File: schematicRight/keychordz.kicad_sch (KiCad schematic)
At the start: 66 parts, among them IC1 MCP73833-BZI_UN, IC2 TPS7A2024PDBVR, IC3 STM32WB55RGV7, J1 USB_C_Receptacle_USB2.0, J2 DEBUG_CONN, J3 OLED_CONN, Q1 Q_PMOS_GSD, SW1 SW_Push, SW2 SW_Push, SW3 SW_Push, SW4 SW_Push, SW5 SW_Push, SW6 SW_Push, SW7 SW_Push, SW9 SW_SPST, U1 MIC5504-3.3YM5, Y1 Crystal_GND23, Y2 Crystal

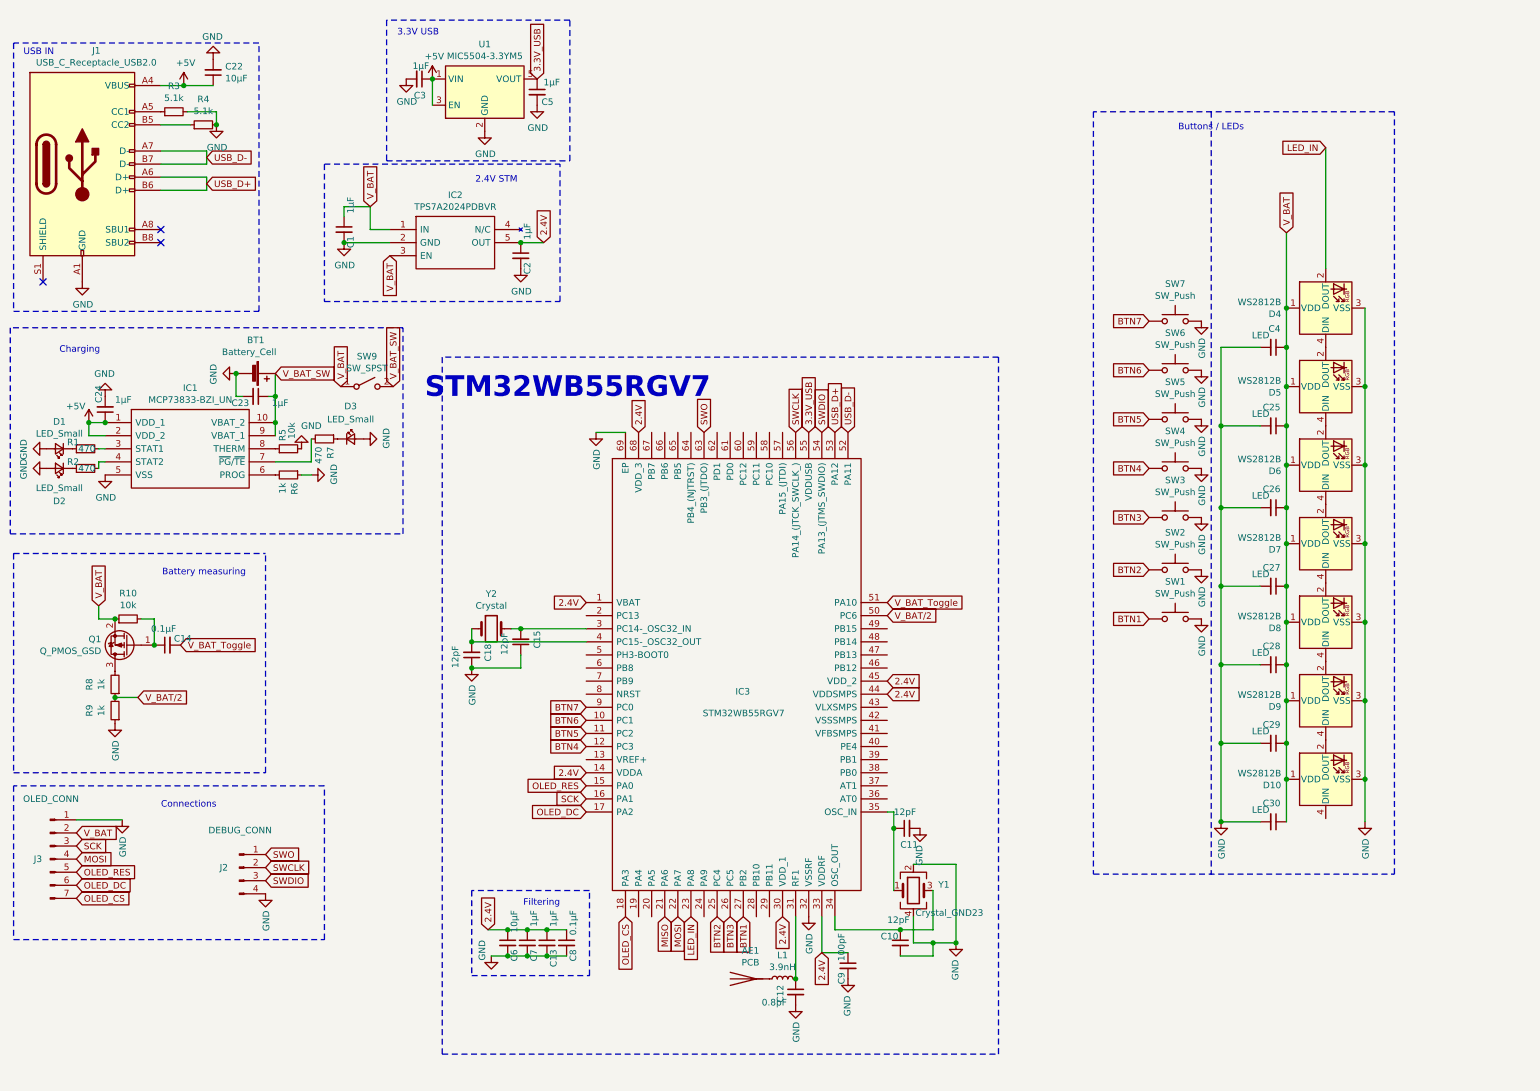
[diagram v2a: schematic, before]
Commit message: use Arduino pro micro
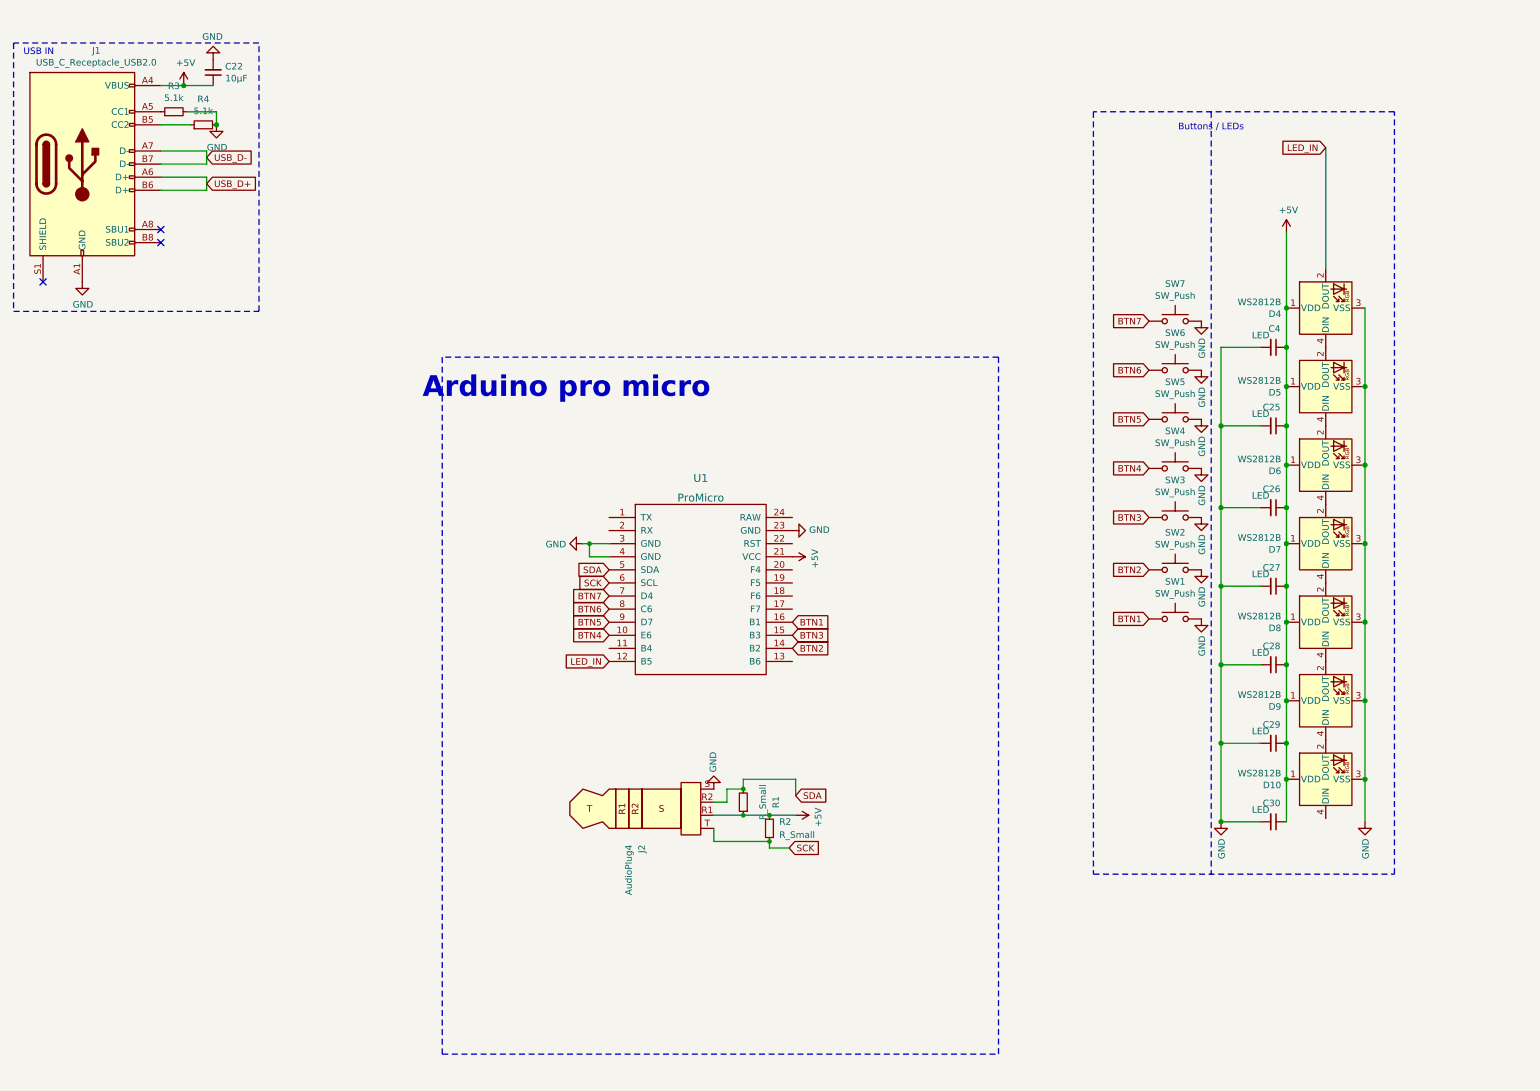
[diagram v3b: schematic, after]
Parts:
- removed AE1: PCB, RF_Antenna:Texas_SWRA117D_2.4GHz_Left, symbol Device:Antenna
- removed BT1: Battery_Cell, Battery:BatteryHolder_MPD_BH-18650-PC2, symbol Device:Battery_Cell
- removed C1, C13, C2, C23, C24, C3, C5, C7: 1µF, Capacitor_SMD:C_0402_1005Metric_Pad0.74x0.62mm_HandSolder, symbol Device:C_Small
- removed C10, C11, C15, C18: 12pF, Capacitor_SMD:C_0603_1608Metric_Pad1.08x0.95mm_HandSolder, symbol Device:C_Small
- removed C12: 0.8pF, Capacitor_SMD:C_0201_0603Metric_Pad0.64x0.40mm_HandSolder, symbol Device:C_Small
- removed C14, C8: 0.1µF, Capacitor_SMD:C_0402_1005Metric_Pad0.74x0.62mm_HandSolder, symbol Device:C_Small
- removed C6: 10µF, Capacitor_SMD:C_0402_1005Metric_Pad0.74x0.62mm_HandSolder, symbol Device:C_Small
- removed C9: 100pF, Capacitor_SMD:C_0402_1005Metric_Pad0.74x0.62mm_HandSolder, symbol Device:C_Small
- removed D1, D2, D3: LED_Small, LED_SMD:LED_0603_1608Metric_Pad1.05x0.95mm_HandSolder, symbol Device:LED_Small
- removed IC1: MCP73833-BZI_UN, Package_SO:MSOP-10_3x3mm_P0.5mm, symbol LoaderParts:MCP73833-BZI_UN
- removed IC2: TPS7A2024PDBVR, SamacSys_Parts:SOT95P280X145-5N, symbol LoaderParts:TPS7A2033PDBVR
- removed IC3: STM32WB55RGV7, SamacSys_Parts:QFN40P800X800X100-69N-D, symbol LoaderParts:STM32WB55RGV7
- removed J2: DEBUG_CONN, Connector_PinHeader_2.54mm:PinHeader_1x04_P2.54mm_Vertical, symbol Connector:Conn_01x04_Male
- removed J3: OLED_CONN, Connector_PinHeader_2.54mm:PinHeader_1x07_P2.54mm_Vertical, symbol Connector:Conn_01x07_Male
- removed L1: 3.9nH, Inductor_SMD:L_0402_1005Metric_Pad0.77x0.64mm_HandSolder, symbol Device:L_Small
- removed Q1: Q_PMOS_GSD, Package_TO_SOT_SMD:SC-59_Handsoldering, symbol Device:Q_PMOS_GSD
- removed R10: 10k, Resistor_SMD:R_0603_1608Metric_Pad0.98x0.95mm_HandSolder, symbol Device:R_Small
- removed R5: 10k, Resistor_SMD:R_0402_1005Metric_Pad0.72x0.64mm_HandSolder, symbol Device:R_Small
- removed R6: 1k, Resistor_SMD:R_0402_1005Metric_Pad0.72x0.64mm_HandSolder, symbol Device:R_Small
- removed R7: 470, Resistor_SMD:R_0603_1608Metric_Pad0.98x0.95mm_HandSolder, symbol Device:R_Small
- removed R8, R9: 1k, Resistor_SMD:R_0603_1608Metric_Pad0.98x0.95mm_HandSolder, symbol Device:R_Small
- removed SW9: SW_SPST, Button_Switch_THT:SW_DIP_SPSTx02_Slide_6.7x6.64mm_W7.62mm_P2.54mm_LowProfile, symbol Switch:SW_SPST
- removed U1: MIC5504-3.3YM5, Package_TO_SOT_SMD:SOT-23-5, symbol Regulator_Linear:MIC5504-3.3YM5
- removed Y1: Crystal_GND23, Crystal:Crystal_SMD_2016-4Pin_2.0x1.6mm_HandSoldering, symbol Device:Crystal_GND24
- removed Y2: Crystal, Crystal:Crystal_SMD_MicroCrystal_CC7V-T1A-2Pin_3.2x1.5mm_HandSoldering, symbol Device:Crystal
- added J2: AudioPlug4, Connector_Audio:Jack_3.5mm_PJ320D_Horizontal, symbol Connector:AudioPlug4
- added U1: ProMicro, promicro:ProMicro, symbol promicro:ProMicro
- R1, R2: value 470 -> R_Small
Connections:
- net V_BAT is gone; now on net +5V: C25.1, C26.1, C27.1, C28.1, C29.1, C30.1, C4.1, D10.1 (VDD), D4.1 (VDD), D5.1 (VDD), D6.1 (VDD), D7.1 (VDD), D8.1 (VDD), D9.1 (VDD)
- net +5V: now also R1.1, R2.2, J2.R1, U1.21 (VCC)
- net BTN1: now also U1.16 (B1)
- net BTN2: now also U1.14 (B2)
- net BTN3: now also U1.15 (B3)
- net BTN4: now also U1.10 (E6)
- net BTN5: now also U1.9 (D7)
- net BTN6: now also U1.8 (C6)
- net BTN7: now also U1.7 (D4)
- net GND: now also J2.S, U1.23 (GND), U1.3 (GND), U1.4 (GND)
- net LED_IN: now also U1.12 (B5)
- net SCK: now also R2.1, J2.T, U1.6 (SCL)
- net SDA: now reaches R1.2
- net SDA: now also J2.R2, U1.5 (SDA)
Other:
- note added: "Arduino pro micro"
- note removed: "2.4V STM"
- note removed: "3.3V USB"
- note removed: "Battery measuring"
- note removed: "Charging"
- note removed: "Connections"
- note removed: "Filtering"
- note removed: "STM32WB55RGV7"

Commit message: fix LED vcc
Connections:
- net +5V: now also U1.24 (RAW); no longer U1.21 (VCC)
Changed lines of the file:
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@@
     (pin "4")
   )
-  (symbol (lib_id "power:+5V") (at 168.91 116.84 270) (unit 1)
+  (symbol (lib_id "power:+5V") (at 168.91 109.22 270) (unit 1)
     (in_bom yes) (on_board yes)
-    (property "Reference" "#PWR0113" (id 0) (at 165.1 116.84 0)
+    (property "Reference" "#PWR0113" (id 0) (at 165.1 109.22 0)
       (effects (font (size 1.27 1.27)) hide)
     )
-    (property "Value" "+5V" (id 1) (at 173.3042 117.221 0))
-    (property "Footprint" "" (id 2) (at 168.91 116.84 0)
+    (property "Value" "+5V" (id 1) (at 173.3042 109.601 0))
+    (property "Footprint" "" (id 2) (at 168.91 109.22 0)
       (effects (font (size 1.27 1.27)) hide)
     )
-    (property "Datasheet" "" (id 3) (at 168.91 116.84 0)
+    (property "Datasheet" "" (id 3) (at 168.91 109.22 0)
       (effects (font (size 1.27 1.27)) hide)
     )

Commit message: add new hardware rev
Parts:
- added SW?: (no value), symbol Switch:SW_Push
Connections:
- net GND: now also SW?.2
- net LED_IN: now also D10.4 (DIN); no longer D4.2 (DOUT)
- net at U1.22 (RST): now also SW?.1
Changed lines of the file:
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@@
   (junction (at 252.095 137.795) (diameter 1.016) (color 0 0 0 0)
+  )
+  (junction (at 180.34 111.76) (diameter 0) (color 0 0 0 0)
   )
   (junction (at 264.795 76.2) (diameter 1.016) (color 0 0 0 0)
@@
     (stroke (width 0) (type solid) (color 0 0 0 0))
   )
+  (wire (pts (xy 272.415 167.64) (xy 272.415 168.91))
+    (stroke (width 0) (type default) (color 0 0 0 0))
+  )
   (wire (pts (xy 280.035 114.3) (xy 280.035 129.54))
     (stroke (width 0) (type solid) (color 0 0 0 0))
@@
   )
   (wire (pts (xy 128.27 114.3) (xy 129.54 114.3))
+    (stroke (width 0) (type default) (color 0 0 0 0))
+  )
+  (wire (pts (xy 180.34 111.76) (xy 180.34 111.125))
     (stroke (width 0) (type default) (color 0 0 0 0))
   )
@@
     (stroke (width 0) (type solid) (color 0 0 0 0))
   )
+  (wire (pts (xy 168.91 114.3) (xy 170.815 114.3))
+    (stroke (width 0) (type default) (color 0 0 0 0))
+  )
   (wire (pts (xy 164.465 167.005) (xy 169.545 167.005))
     (stroke (width 0) (type default) (color 0 0 0 0))
@@
     (stroke (width 0) (type default) (color 0 0 0 0))
   )
+  (wire (pts (xy 170.815 114.3) (xy 170.815 115.57))
+    (stroke (width 0) (type default) (color 0 0 0 0))
+  )
   (polyline (pts (xy 65.405 69.215) (xy 65.405 17.145))
     (stroke (width 0) (type dash) (color 0 0 0 0))
@@
     (stroke (width 0) (type default) (color 0 0 0 0))
   )
+  (wire (pts (xy 180.975 115.57) (xy 180.975 111.76))
+    (stroke (width 0) (type default) (color 0 0 0 0))
+  )
   (wire (pts (xy 280.035 68.58) (xy 280.035 83.82))
     (stroke (width 0) (type solid) (color 0 0 0 0))
@@
     (stroke (width 0) (type solid) (color 0 0 0 0))
   )
-  (wire (pts (xy 272.415 37.465) (xy 272.415 60.96))
-    (stroke (width 0) (type solid) (color 0 0 0 0))
-  )
   (wire (pts (xy 156.21 161.925) (xy 159.385 161.925))
     (stroke (width 0) (type default) (color 0 0 0 0))
@@
     (stroke (width 0) (type default) (color 0 0 0 0))
   )
+  (wire (pts (xy 180.975 111.76) (xy 180.34 111.76))
+    (stroke (width 0) (type default) (color 0 0 0 0))
+  )
   (wire (pts (xy 159.385 167.005) (xy 164.465 167.005))
     (stroke (width 0) (type default) (color 0 0 0 0))
   )
   (wire (pts (xy 133.35 116.84) (xy 129.54 116.84))
+    (stroke (width 0) (type default) (color 0 0 0 0))
+  )
+  (wire (pts (xy 168.91 111.76) (xy 180.34 111.76))
     (stroke (width 0) (type default) (color 0 0 0 0))
   )
@@
     )
   )
-  (global_label "LED_IN" (shape input) (at 272.415 37.465 180)
-    (effects (font (size 1.27 1.27)) (justify right))
-    (property "Intersheet References" "${INTERSHEET_REFS}" (id 0) (at 263.6519 37.3856 0)
+  (global_label "LED_IN" (shape input) (at 272.415 168.91 270)
+    (effects (font (size 1.27 1.27)) (justify right))
+    (property "Intersheet References" "${INTERSHEET_REFS}" (id 0) (at 272.3356 177.6731 90)
       (effects (font (size 1.27 1.27)) (justify right) hide)
     )
@@
     )
     (property "Datasheet" "~" (id 3) (at 262.255 137.795 0)
+      (effects (font (size 1.27 1.27)) hide)
+    )
+    (pin "1")
+    (pin "2")
+  )
+  (symbol (lib_id "Switch:SW_Push") (at 175.895 115.57 0) (unit 1)
+    (in_bom yes) (on_board yes) (fields_autoplaced)
+    (property "Reference" "SW?" (id 0) (at 175.895 107.95 0))
+    (property "Value" "" (id 1) (at 175.895 110.49 0))
+    (property "Footprint" "" (id 2) (at 175.895 110.49 0)
+      (effects (font (size 1.27 1.27)) hide)
+    )
+    (property "Datasheet" "~" (id 3) (at 175.895 110.49 0)
       (effects (font (size 1.27 1.27)) hide)
     )
@@
     (pin "1")
   )
-  (symbol (lib_id "power:GND") (at 168.91 111.76 90) (unit 1)
-    (in_bom yes) (on_board yes)
-    (property "Reference" "#PWR0112" (id 0) (at 175.26 111.76 0)
-      (effects (font (size 1.27 1.27)) hide)
-    )
-    (property "Value" "GND" (id 1) (at 172.1612 111.633 90)
-      (effects (font (size 1.27 1.27)) (justify right))
-    )
-    (property "Footprint" "" (id 2) (at 168.91 111.76 0)
-      (effects (font (size 1.27 1.27)) hide)
-    )
-    (property "Datasheet" "" (id 3) (at 168.91 111.76 0)
+  (symbol (lib_id "power:GND") (at 180.34 111.125 180) (unit 1)
+    (in_bom yes) (on_board yes)
+    (property "Reference" "#PWR0112" (id 0) (at 180.34 104.775 0)
+      (effects (font (size 1.27 1.27)) hide)
+    )
+    (property "Value" "GND" (id 1) (at 180.213 107.8738 90)
+      (effects (font (size 1.27 1.27)) (justify right))
+    )
+    (property "Footprint" "" (id 2) (at 180.34 111.125 0)
+      (effects (font (size 1.27 1.27)) hide)
+    )
+    (property "Datasheet" "" (id 3) (at 180.34 111.125 0)
       (effects (font (size 1.27 1.27)) hide)
     )
@@
       (reference "SW7") (unit 1) (value "SW_Push") (footprint "schematic:SW_PG1350")
     )
+    (path "/18c5a2e9-5477-4075-9795-9d29ce509901"
+      (reference "SW?") (unit 1) (value "SW_Push") (footprint "")
+    )
     (path "/4c95f4c3-e715-45e3-946c-f27355a4d041"
